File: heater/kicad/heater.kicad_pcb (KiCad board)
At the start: 2 copper layers, 90 x 88.4 mm, 85 parts, among them J1 Conn_01x02_Pin, J2 Conn_01x02_Pin, J3 pcie_98, U1 OPA863SIDBVR, U11 ESD5344D-TP, U12 ESD5344D-TP, U13 XC6206P332MR, U15 TPS7A2025PDBVR, U2 D050505T-1WR4, U3 LTC1966, U5 TPS72325DBVR, U6 LTC1966, U8 ADS1115IDGS, U9 ISO1541

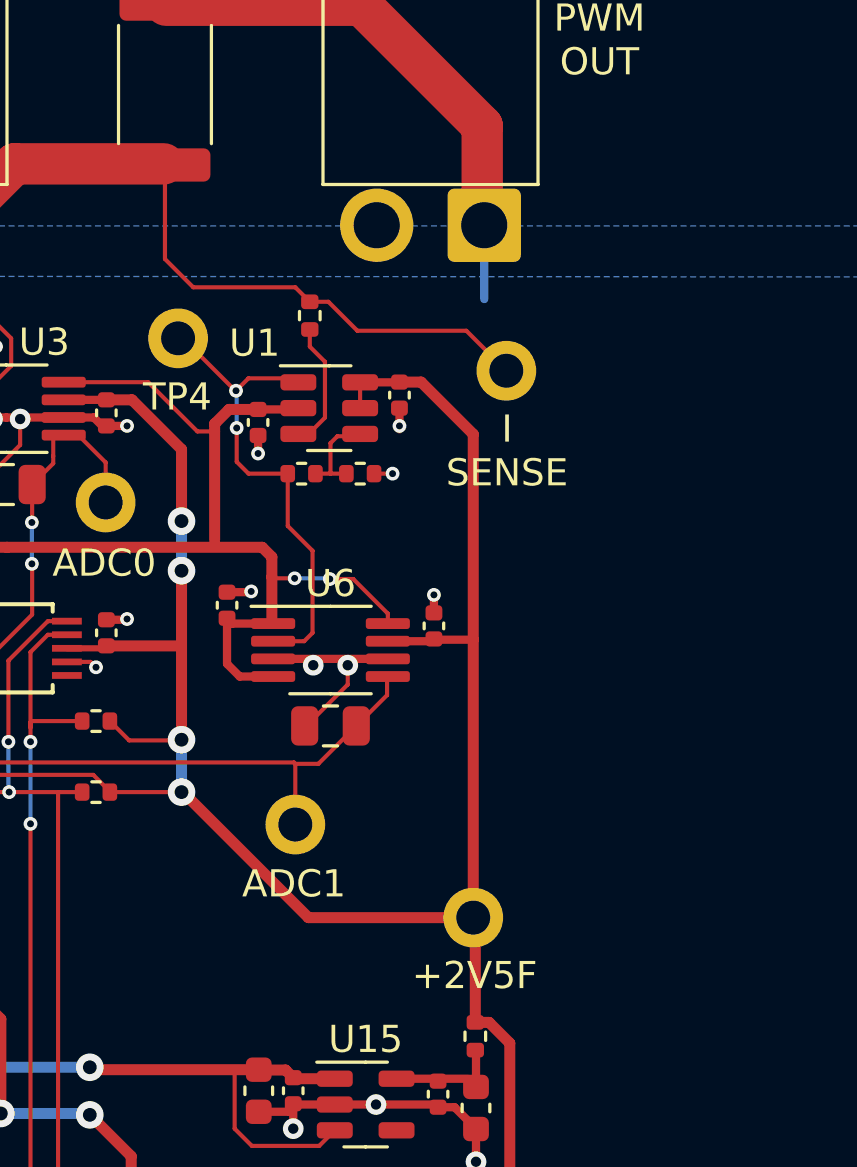
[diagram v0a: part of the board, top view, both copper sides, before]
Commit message: Changed the I sense op amp to a low bias current one.
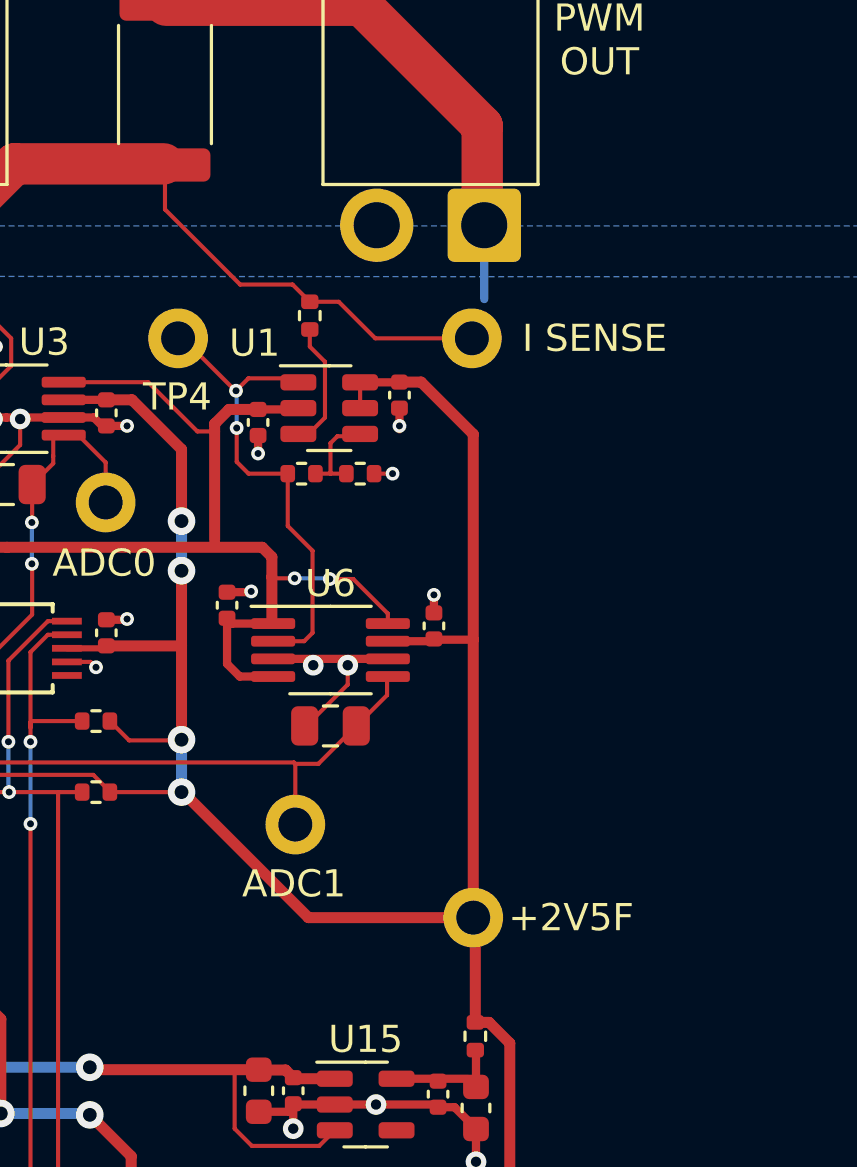
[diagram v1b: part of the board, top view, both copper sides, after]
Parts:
- U1: value OPA863SIDBVR -> OPA810IDBV
- moved TP3 1.74 mm to (38.7, -72.8)
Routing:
- net /I_SENSE: track 48.7 -> 45.9 mm
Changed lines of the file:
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@@
   )
   (footprint "common:Test_Pad" (layer "F.Cu")
-    (at 40.005 -71.628)
+    (at 38.735 -72.8218)
     (descr "Through hole straight pin header, 1x02, 2.54mm pitch, single row")
     (tags "Through hole pin header THT 1x02 2.54mm single row")
@@
     (descr "TSOT, 6 Pin (https://www.jedec.org/sites/default/files/docs/MO-193D.pdf variant AA), generated with kicad-footprint-generator ipc_gullwing_generator.py")
     (tags "TSOT TO_SOT_SMD")
-    (property "LCSC" "C4369756")
+    (property "LCSC" "C2833513")
     (property "Sheetfile" "heater.kicad_sch")
     (property "Sheetname" "")
@@
         (effects (font (size 1 1) (thickness 0.15)))
     )
-    (fp_text value "OPA863SIDBVR" (at 0 2.4) (layer "F.Fab")
+    (fp_text value "OPA810IDBV" (at 0 2.4) (layer "F.Fab")
         (effects (font (size 1 1) (thickness 0.15)))
     )
@@
     (effects (font (size 1 1) (thickness 0.15)) (justify bottom mirror))
   )
-  (gr_text "+2V5F" (at 38.862 -48.768) (layer "B.SilkS")
-    (effects (font (size 1 1) (thickness 0.15)) (justify bottom mirror))
+  (gr_text "+2V5F" (at 42.5704 -51.4858) (layer "B.SilkS")
+    (effects (font (size 1 1) (thickness 0.15)) (justify mirror))
   )
-  (gr_text "I\nSENSE" (at 40.005 -67.31) (layer "B.SilkS")
-    (effects (font (size 1 1) (thickness 0.15)) (justify bottom mirror))
+  (gr_text "I SENSE" (at 43.3578 -72.8218) (layer "B.SilkS")
+    (effects (font (size 1 1) (thickness 0.15)) (justify mirror))
   )
   (gr_text "+3V3" (at 32.258 -10.541) (layer "B.SilkS")
@@
     (effects (font (size 1 1) (thickness 0.15)) (justify left bottom))
   )
-  (gr_text "+2V5F" (at 38.8366 -48.768) (layer "F.SilkS")
-    (effects (font (size 1 1) (thickness 0.15)) (justify bottom))
+  (gr_text "+2V5F" (at 42.3926 -51.4858) (layer "F.SilkS")
+    (effects (font (size 1 1) (thickness 0.15)))
   )
   (gr_text "ADC0" (at 25.1968 -63.9572) (layer "F.SilkS")
@@
     (effects (font (size 1.778 1.524) (thickness 0.2286)) (justify left bottom))
   )
-  (gr_text "I\nSENSE" (at 40.0304 -67.2846) (layer "F.SilkS")
-    (effects (font (size 1 1) (thickness 0.15)) (justify bottom))
+  (gr_text "I SENSE" (at 43.2562 -72.8218) (layer "F.SilkS")
+    (effects (font (size 1 1) (thickness 0.15)))
   )
   (segment (start -11.303 -17.272) (end -11.684 -16.891) (width 0.4064) (layer "F.Cu") (net 1))
@@
   (via (at 30.0482 -70.8914) (size 0.508) (drill 0.254) (layers "F.Cu" "B.Cu") (net 112))
   (segment (start 30.0736 -70.8406) (end 30.0736 -69.5198) (width 0.1524) (layer "B.Cu") (net 112))
-  (segment (start 34.5186 -73.1012) (end 38.5318 -73.1012) (width 0.1524) (layer "F.Cu") (net 113))
-  (segment (start 33.4518 -74.168) (end 34.5186 -73.1012) (width 0.1524) (layer "F.Cu") (net 113))
+  (segment (start 32.766 -74.168) (end 33.8328 -74.168) (width 0.1524) (layer "F.Cu") (net 113))
+  (segment (start 27.432 -79.2065) (end 27.432 -77.5716) (width 0.1524) (layer "F.Cu") (net 113))
+  (segment (start 32.131 -74.803) (end 32.766 -74.168) (width 0.1524) (layer "F.Cu") (net 113))
   (segment (start 21.894 -79.248) (end 27.3905 -79.248) (width 1.524) (layer "F.Cu") (net 113))
-  (segment (start 27.432 -79.2065) (end 27.432 -75.7428) (width 0.1524) (layer "F.Cu") (net 113))
+  (segment (start 27.432 -77.5716) (end 30.2006 -74.803) (width 0.1524) (layer "F.Cu") (net 113))
   (segment (start 18.1864 -79.5782) (end 14.0716 -79.5782) (width 0.1524) (layer "F.Cu") (net 113))
   (segment (start 4.338 -69.8446) (end 4.338 -68.605) (width 0.1524) (layer "F.Cu") (net 113))
   (segment (start 18.8722 -78.8924) (end 18.1864 -79.5782) (width 0.1524) (layer "F.Cu") (net 113))
-  (segment (start 32.2326 -74.7014) (end 32.766 -74.168) (width 0.1524) (layer "F.Cu") (net 113))
+  (segment (start 35.179 -72.8218) (end 38.735 -72.8218) (width 0.1524) (layer "F.Cu") (net 113))
   (segment (start 19.633 -76.987) (end 18.8722 -77.7478) (width 0.1524) (layer "F.Cu") (net 113))
   (segment (start 14.0716 -79.5782) (end 4.338 -69.8446) (width 0.1524) (layer "F.Cu") (net 113))
-  (segment (start 32.766 -74.168) (end 33.4518 -74.168) (width 0.1524) (layer "F.Cu") (net 113))
   (segment (start 18.8722 -77.7478) (end 18.8722 -78.8924) (width 0.1524) (layer "F.Cu") (net 113))
+  (segment (start 33.8328 -74.168) (end 35.179 -72.8218) (width 0.1524) (layer "F.Cu") (net 113))
+  (segment (start 30.2006 -74.803) (end 32.131 -74.803) (width 0.1524) (layer "F.Cu") (net 113))
   (segment (start 19.633 -76.987) (end 21.894 -79.248) (width 1.524) (layer "F.Cu") (net 113))
-  (segment (start 27.432 -75.7428) (end 28.4734 -74.7014) (width 0.1524) (layer "F.Cu") (net 113))
-  (segment (start 38.5318 -73.1012) (end 40.005 -71.628) (width 0.1524) (layer "F.Cu") (net 113))
-  (segment (start 28.4734 -74.7014) (end 32.2326 -74.7014) (width 0.1524) (layer "F.Cu") (net 113))
   (segment (start 23.495 -56.0832) (end 23.5204 -56.1086) (width 0.1524) (layer "F.Cu") (net 114))
   (segment (start 15.115 -59.309) (end 15.115 -58.289) (width 0.1524) (layer "F.Cu") (net 114))
@@
     )
   )
-  (group "" (id d5da46ea-899f-44d1-91dd-7e951bd0c498)
+  (group "" (id a08a3d90-8258-403f-9f8b-b744561acab2)
     (members
-      50b7681f-d259-44ca-b4c9-f13e662dc49c
       e15e3dcd-2041-42e6-a1d2-4559a6091d71
       ec5e0fc4-7a0e-4c60-9174-9a2446aed991

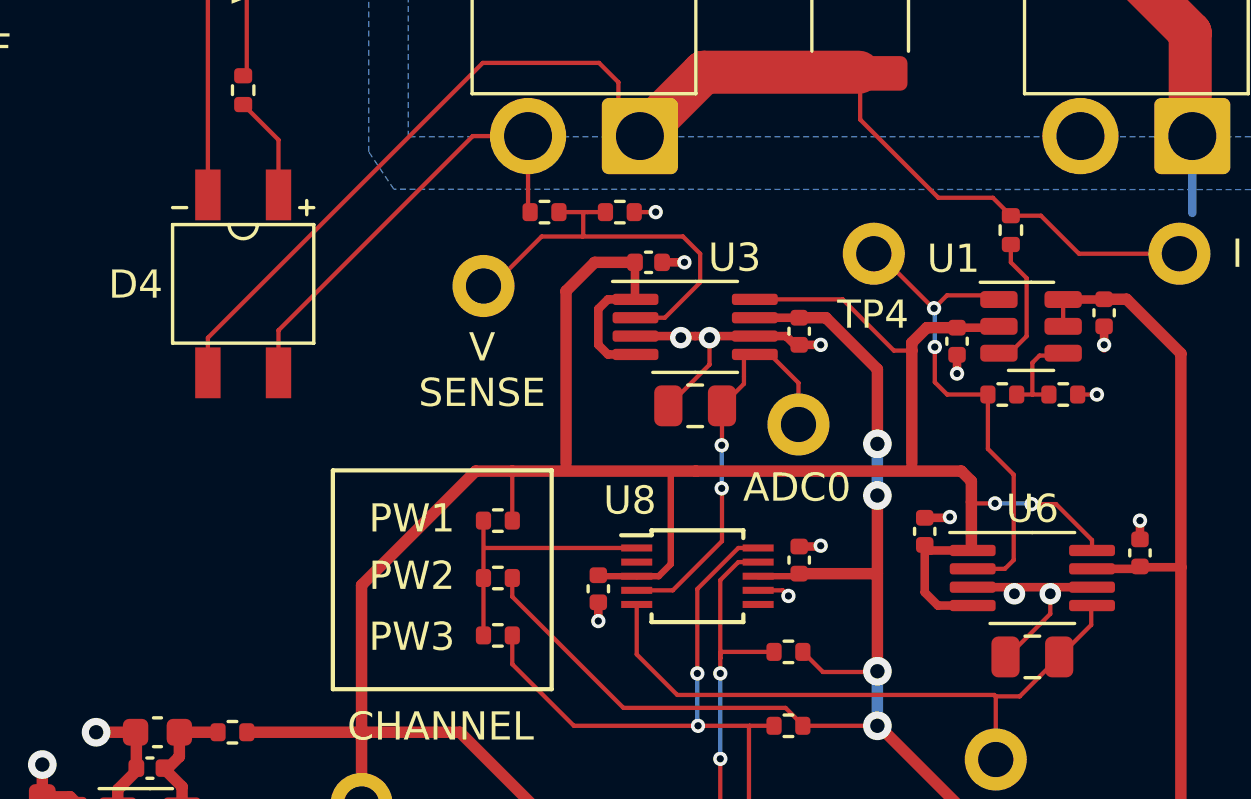
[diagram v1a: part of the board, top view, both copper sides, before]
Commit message: Verified footprints and pinouts. (Recovered from a bad merge)
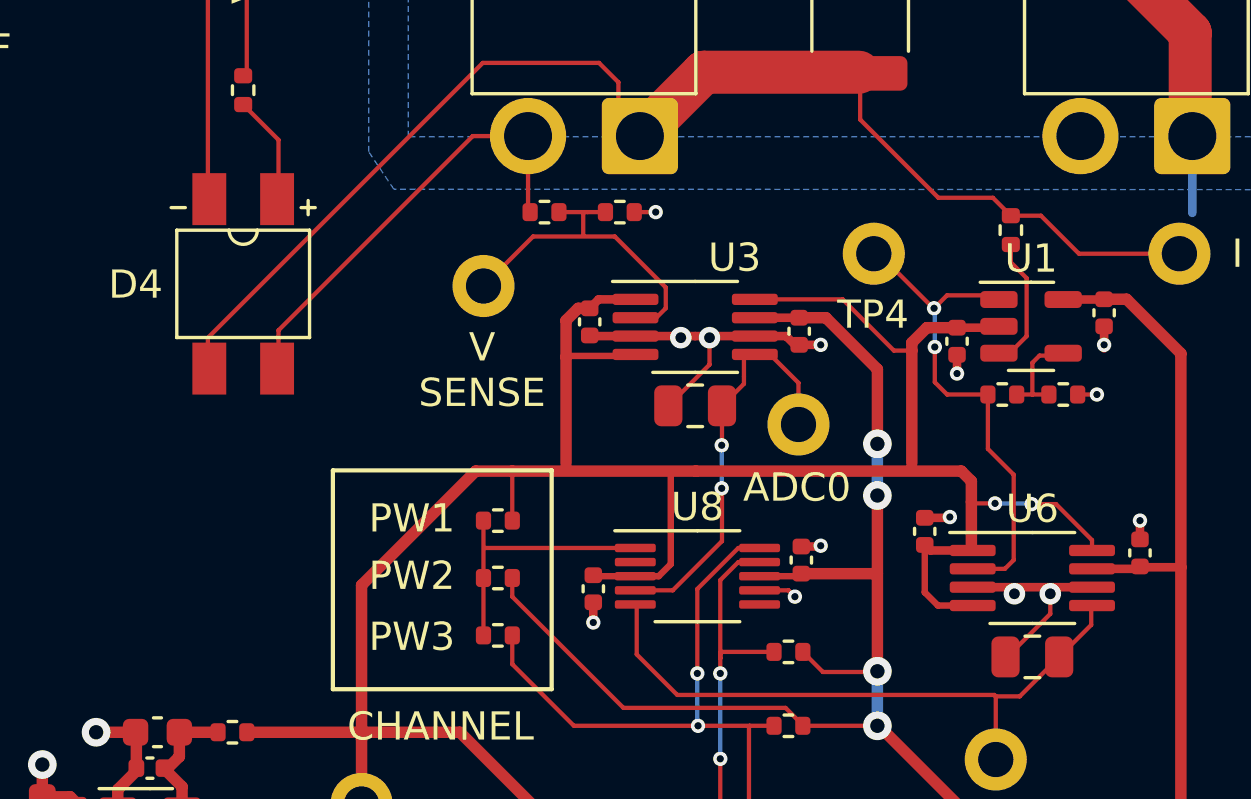
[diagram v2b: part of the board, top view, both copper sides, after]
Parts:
- U1: value OPA810IDBV -> OPA810IDBVT; footprint Package_TO_SOT_SMD:TSOT-23-6 -> Package_TO_SOT_SMD:TSOT-23-5
- U8: footprint Package_SO:TSSOP-10_3x3mm_P0.5mm -> Package_SO:VSSOP-10_3x3mm_P0.5mm
- moved C7 2.96 mm to (17.9, -70.4), turned to -90 degrees
- moved C37 0.18 mm to (18.0, -61.0)
- moved C13 0.08 mm to (25.3, -62.0)
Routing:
- net -2V5F: track 132.9 -> 128.9 mm
- net /V_SENSE: track 15.0 -> 12.4 mm
- net GNDF: track 86.7 -> 87.7 mm, vias 27 -> 26
- net +2V5F: track 128.7 -> 127.8 mm

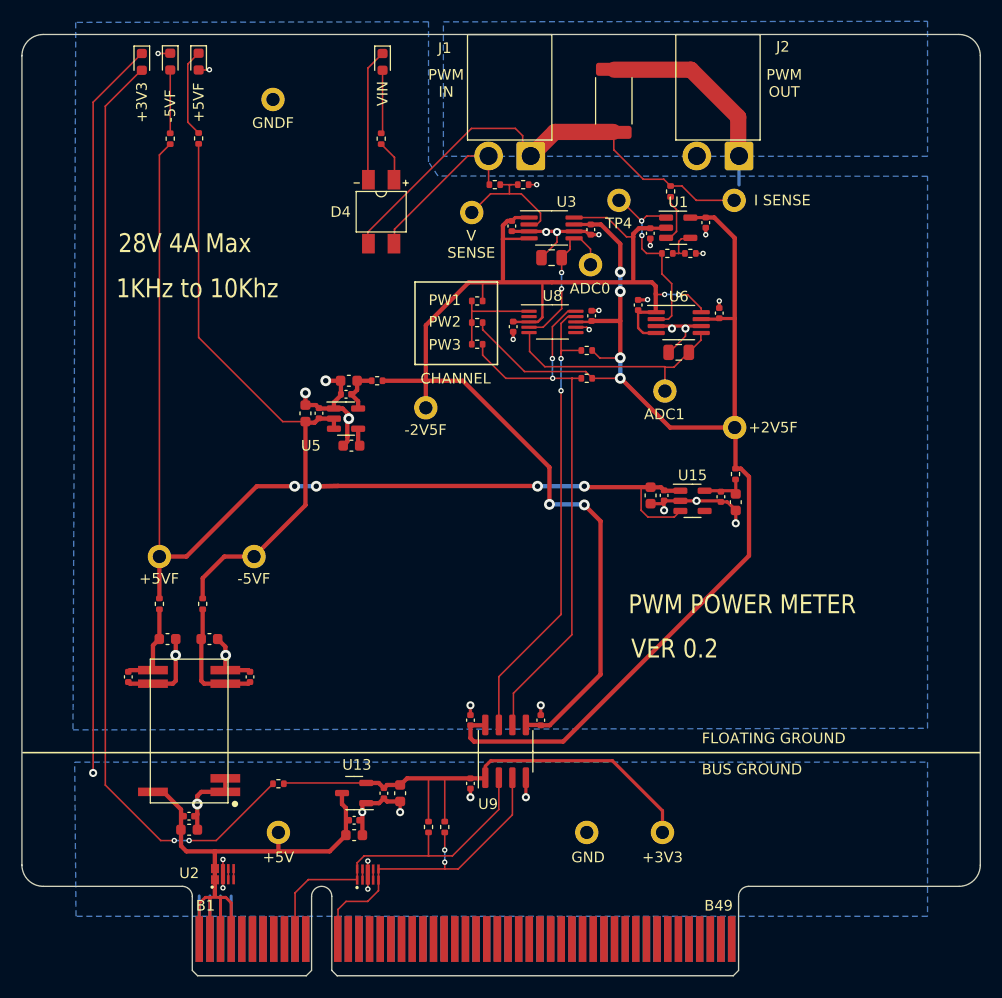
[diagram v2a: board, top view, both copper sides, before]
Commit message: Added an indicator led for reversed VIN.
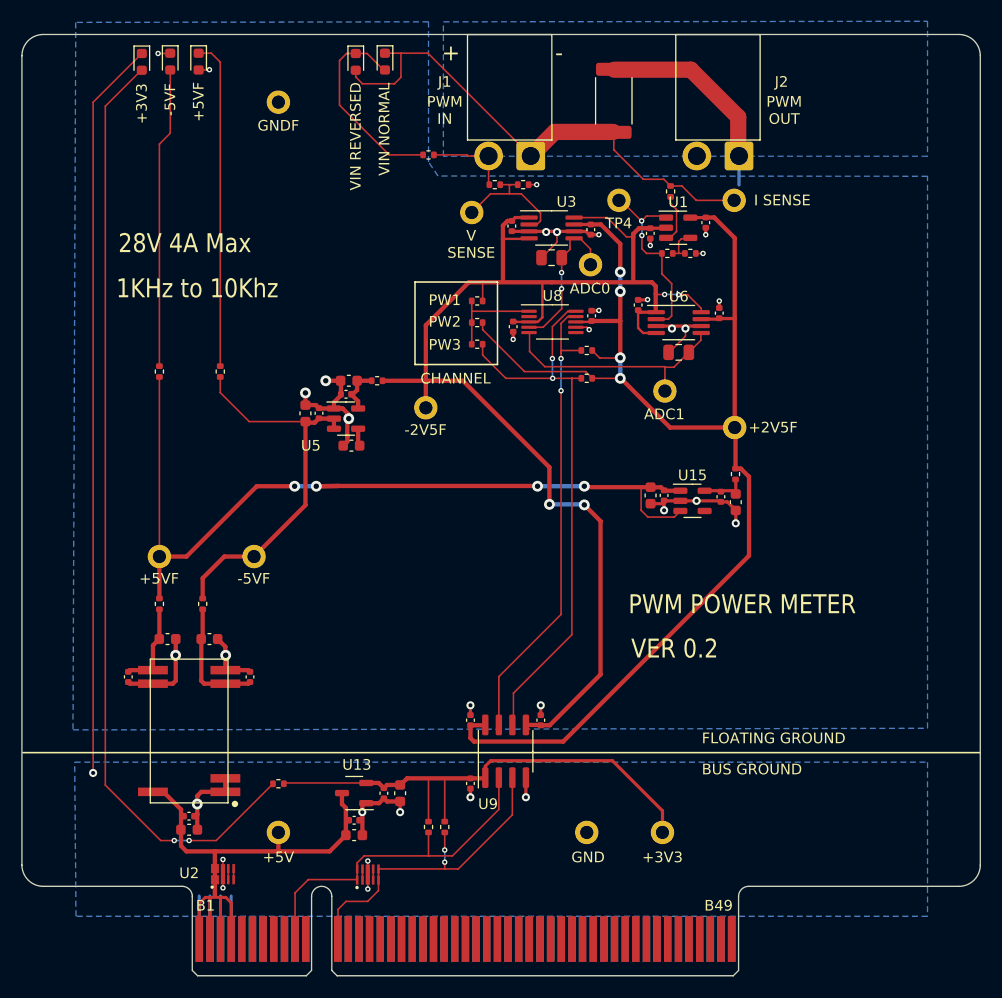
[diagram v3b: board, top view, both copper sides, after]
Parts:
- D4: value MBS10S -> YEL; footprint common:Diode_Bridge_MBS10 -> LED_SMD:LED_0603_1608Metric
- moved R5 22.0 mm to (-9.53, -56.7)
- moved R7 21.9 mm to (-15.2, -56.7)
- moved D4 14.3 mm to (3.20, -85.8), turned to -90 degrees
- moved R12 4.70 mm to (10.0, -77.1), turned to 180 degrees
- moved TP1 0.57 mm to (-4.06, -82.0)
- moved D5 0.23 mm to (5.94, -85.9)
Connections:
- D4 pad 1: Net-(D4-+) -> Net-(D4-K)
- D4 pad 2: Net-(D4--) -> /I_SENSE
- D5 pad 1: Net-(D4--) -> /I_SENSE
- D5 pad 2: Net-(D5-A) -> Net-(D4-K)
- R12 pad 1: Net-(D4-+) -> /VIN
- R12 pad 2: Net-(D5-A) -> Net-(D4-K)
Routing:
- net Net-(D1-K): track 8.33 -> 30.9 mm
- net +5VF: track 102.9 -> 80.6 mm
- net Net-(D2-A): track 5.94 -> 28.2 mm
- net -5VF: track 57.6 -> 36.7 mm
- net Net-(D4-K): track 0.00 -> 19.2 mm
- net Net-(D4--): track 12.3 -> 0.00 mm
- net /VIN: track 16.0 -> 7.95 mm
- net Net-(D5-A): track 5.97 -> 0.00 mm
- net Net-(D4-+): track 3.72 -> 0.00 mm
- net /I_SENSE: track 45.9 -> 48.9 mm
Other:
- board text added: "+"
- board text added: "-"
- board text added: "VIN NORMAL"
- board text added: "VIN REVERSED"
- board text removed: "VIN"

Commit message: Tweaked the vin indicator.
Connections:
- net /I_SENSE renamed /-I_SENSE
